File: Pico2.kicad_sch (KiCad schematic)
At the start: 38 parts, among them J1 DE15_Pins_HighDensity, J10 Conn_02x10_Odd_Even, J11 DB25_Socket, J3 Conn_02x04_Odd_Even, J5 Micro_SD_Card, J8 W5500 Lite, J9 DB25_Pins, U1 RASPBERRY_PI_PICO, U2 SN74LVC8T245, U4 74AHCT125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

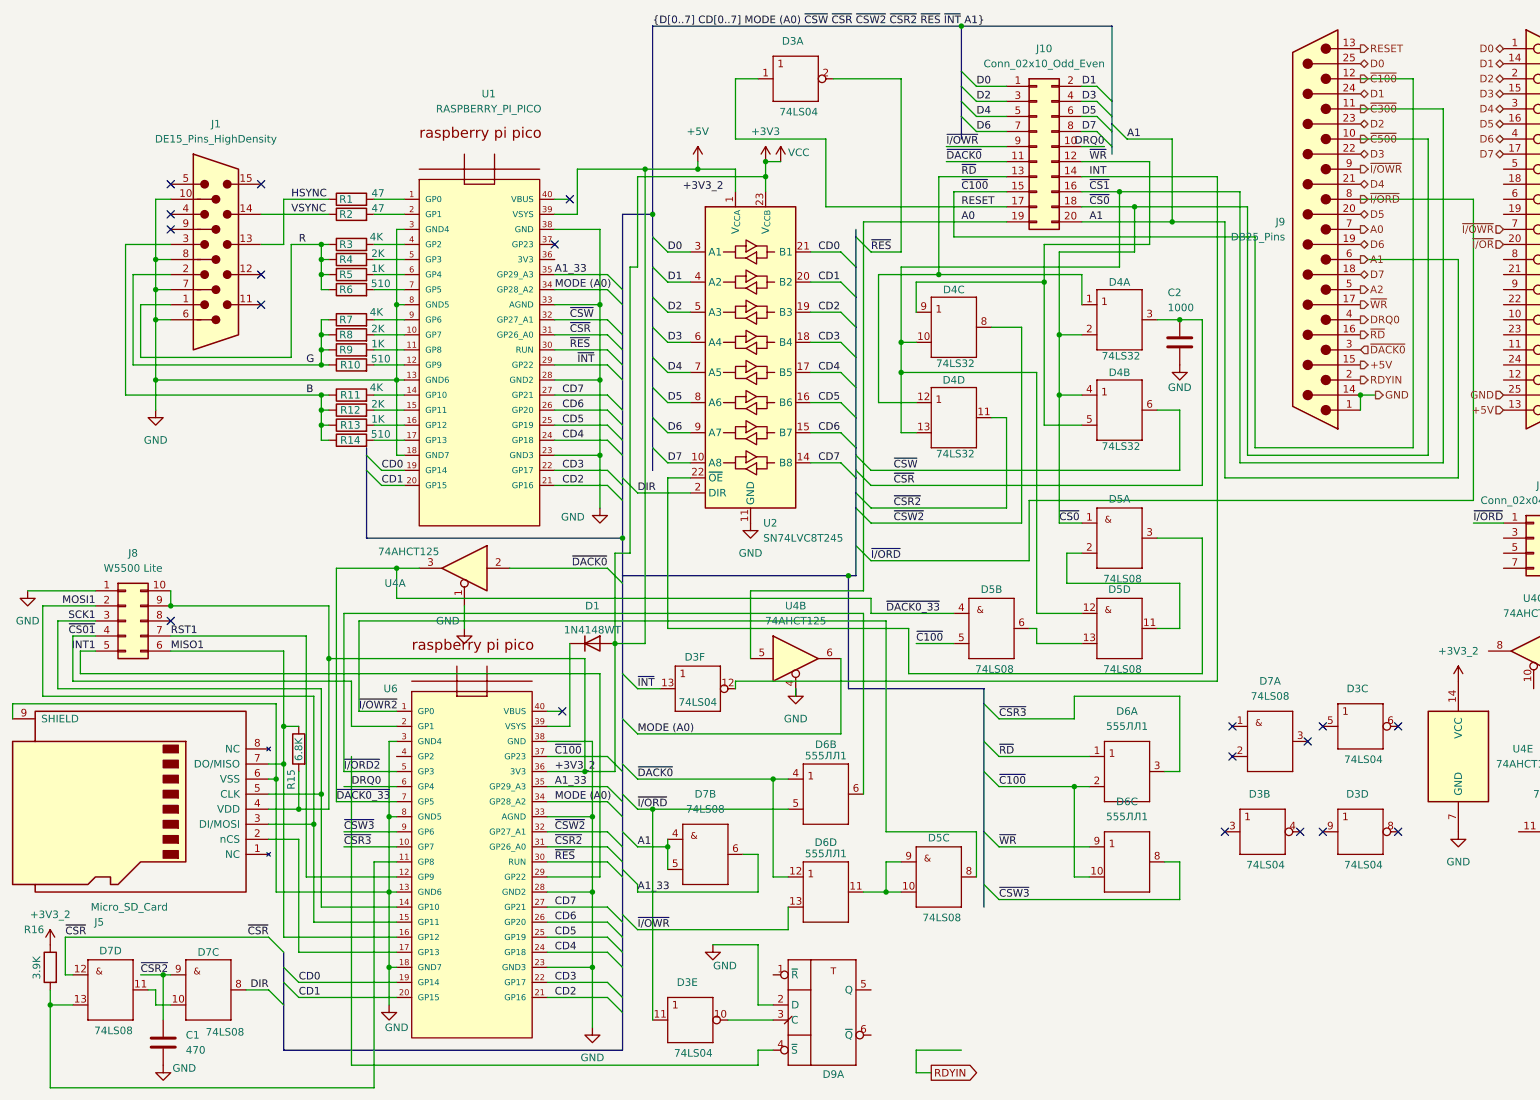
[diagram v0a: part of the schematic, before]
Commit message: Add PicoPDC
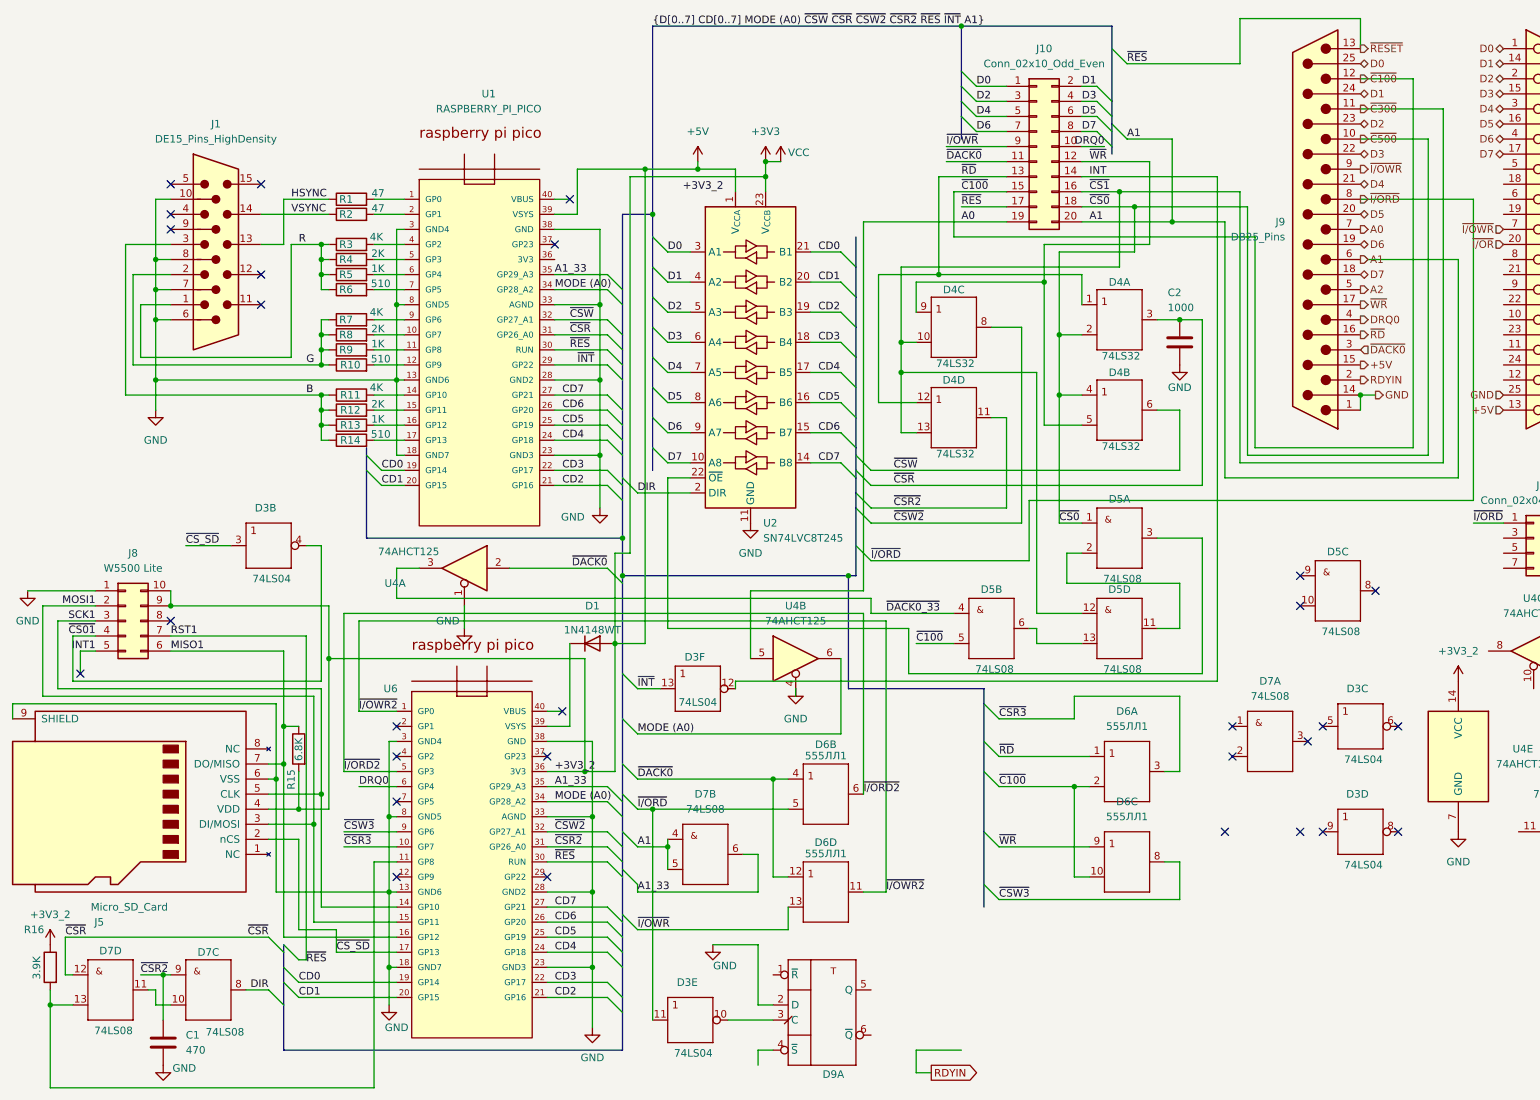
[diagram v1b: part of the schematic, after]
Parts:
- removed unit 1 of D3
- D3: DESCRIPTION (none) -> Hex Schmitt-Trigger INVERTERS
- D4, D6: DESCRIPTION (none) -> Quadruple 2-Input Positive-OR Gates
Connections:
- net ~{RES} is gone; now on net ~{RESET}: U1.30 (RUN), U6.30 (RUN)
- net DRQ0: no longer D9.4 (~{S})
- net INT1: no longer U6.29 (GP22)
- net ~{C100}: no longer U6.37 (GP23)
- net ~{CS01}: now also D3.4 (Y); no longer U6.2 (GP1)
- net ~{DACK0_33}: no longer U6.7 (GP5)
- net ~{I/OWR2}: now also D6.11 (Y); no longer D5.8 (Y)
- net ~{CS_SD}: now reaches J5.2 (nCS), U6.17 (GP13)
- net ~{CS_SD}: now also D3.3 (A)
- net RESET renamed ~{RESET}
- net ~{RESET}: now also J8.7 (Pin_7)
- net RST1: no longer names the net of U6.12 (GP9)
- net RST1: no longer J8.7 (Pin_7)
- now unconnected: D5.10 (B), D5.9 (A)
- no-connect marks 19 -> 29
